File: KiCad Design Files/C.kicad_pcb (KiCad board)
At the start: 2 copper layers, 40.6 x 21.6 mm, 18 parts, among them Q1 2N3904, Q2 2N3904

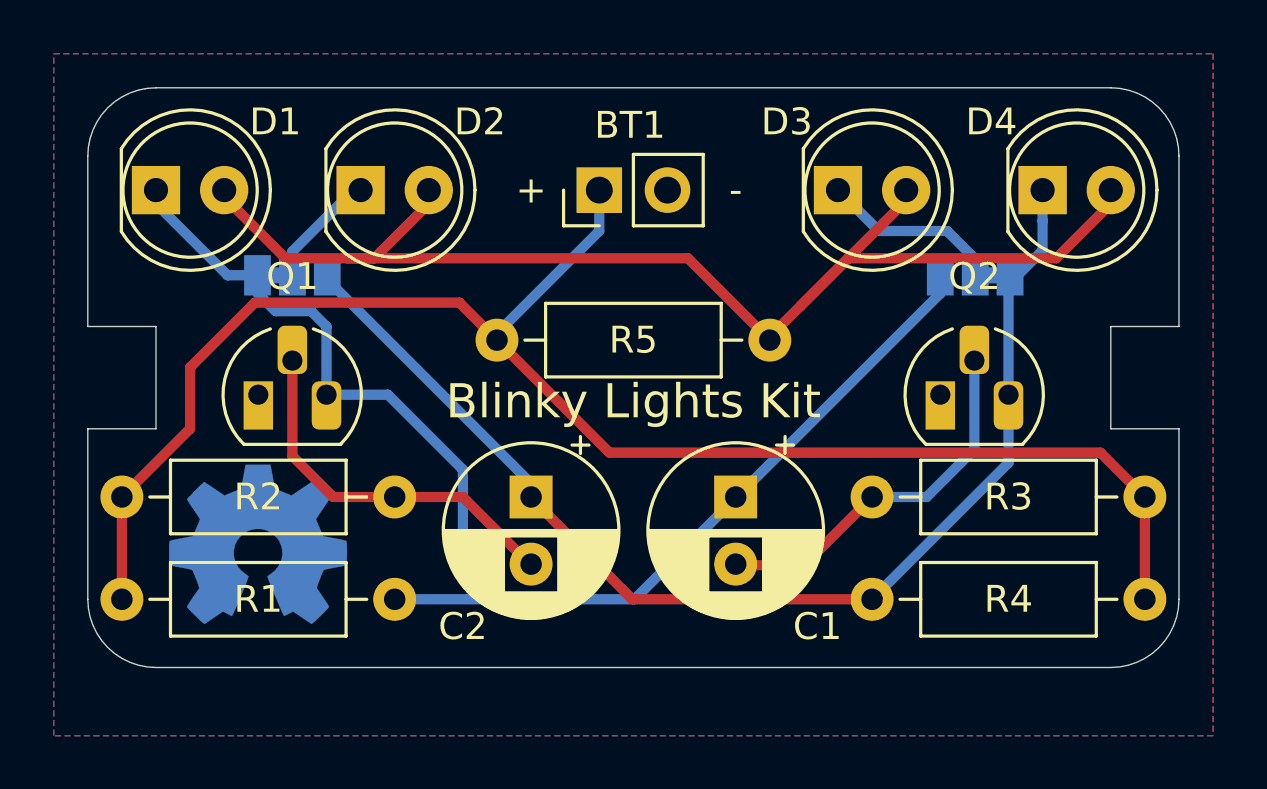
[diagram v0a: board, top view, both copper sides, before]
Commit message: Updated files to KiCAD 6.0 and updated board to rev 1.1
Rev 1.1 includes the following changes:
- Minor silkscreen changes and component movement
- Mainly changed the TO92 package to one which is easier to solder
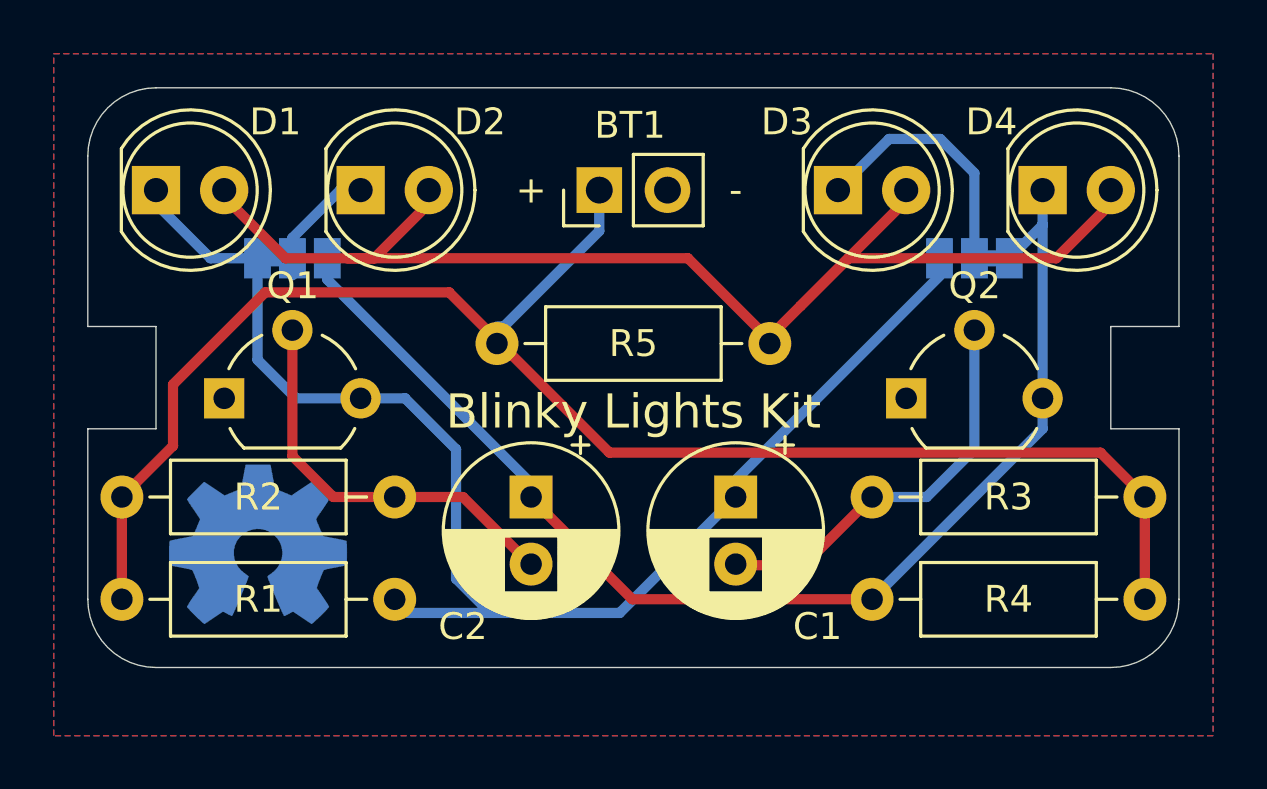
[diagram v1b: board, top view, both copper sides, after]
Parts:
- Q1, Q2: footprint Package_TO_SOT_THT:TO-92_HandSolder -> Package_TO_SOT_THT:TO-92_Wide
- R2, R3: value 100k -> 10k
- moved Q1 1.28 mm to (143.5, 89.0)
- moved Q2 1.28 mm to (168.9, 89.0)
- moved JP2 0.64 mm to (171.4, 83.8)
- moved JP1 0.64 mm to (146.1, 83.8)
- moved R5 0.13 mm to (153.7, 87.0)
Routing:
- net Net-(D3-Pad1): track 6.78 -> 9.57 mm
- net C2: track 43.7 -> 45.4 mm
- net C1: track 48.9 -> 50.4 mm
- net Net-(C2-Pad2): track 14.1 -> 15.3 mm
- net Net-(C1-Pad2): track 14.0 -> 15.1 mm
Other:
- net class Default removed
- board text added: "Rev 1.1"

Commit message: Updated Gerber files for Rev1.1. Added a car enclosure and assembly drawing
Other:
- rule pad_to_mask_clearance: 0.051 -> 0
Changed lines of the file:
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@@
       (dielectric_constraints no)
     )
-    (pad_to_mask_clearance 0.051)
-    (solder_mask_min_width 0.25)
+    (pad_to_mask_clearance 0)
     (pcbplotparams
       (layerselection 0x00010f0_ffffffff)

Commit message: Added a JLCJLCJLCJLC silkscreen for ordering from JLC Removed Gerber and SVG files from git tracking KiCad updated some file's syntax and internal version to latest 6.x
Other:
- board text added: "JLCJLCJLCJLC"
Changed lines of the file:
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@@
     (effects (font (size 1.27 1.27) (thickness 0.1524)) (justify mirror))
+  )
+  (gr_text "JLCJLCJLCJLC" (at 158.75 97.79) (layer "B.SilkS")
+    (effects (font (size 1.27 1.27) (thickness 0.2286)) (justify mirror))
   )
   (gr_text "+" (at 154.94 81.28) (layer "F.SilkS")
